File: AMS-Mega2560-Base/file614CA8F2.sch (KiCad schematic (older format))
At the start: 18 parts, among them IC10 LM2917N-8_NOPB, IC9 MAX764CPA+, J20 Conn_01x02, J21 Conn_01x02

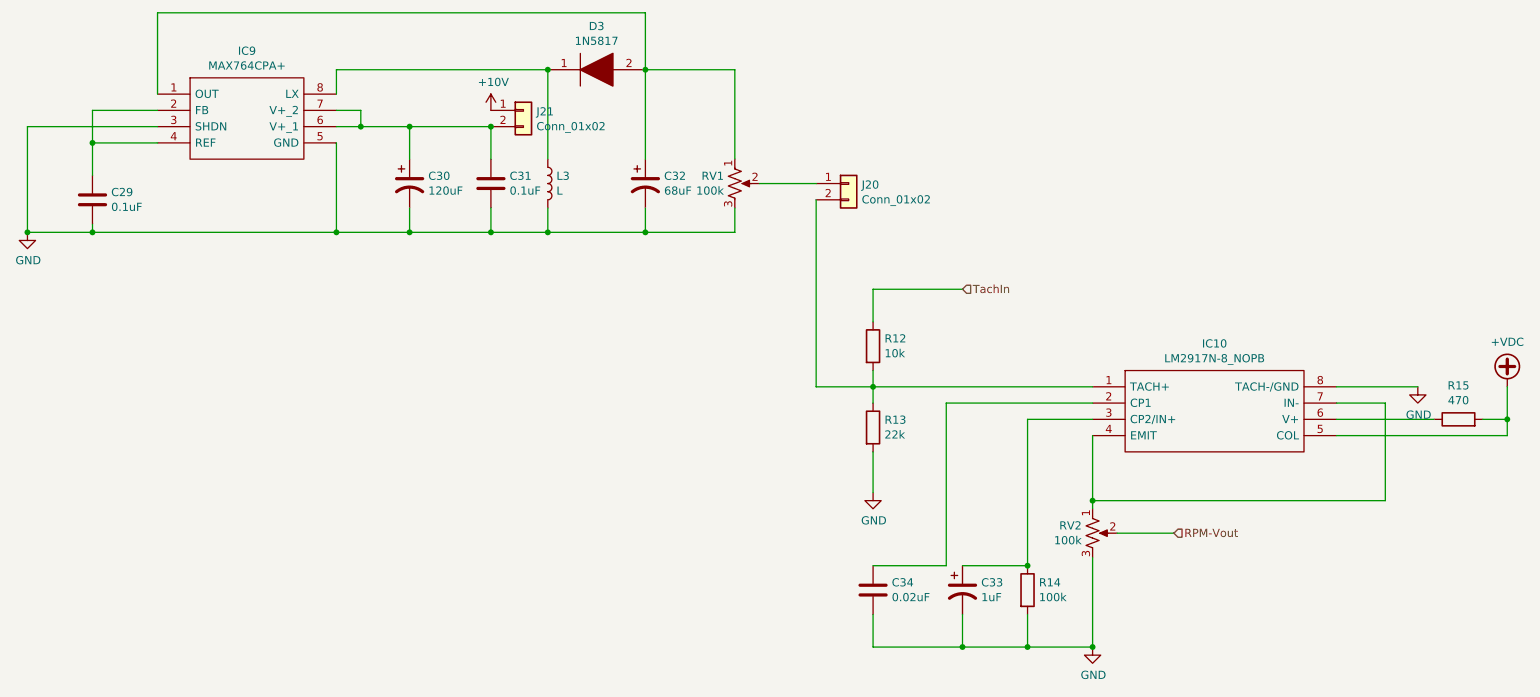
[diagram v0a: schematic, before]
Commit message: rearranging some of the hw design before i rename the repo.
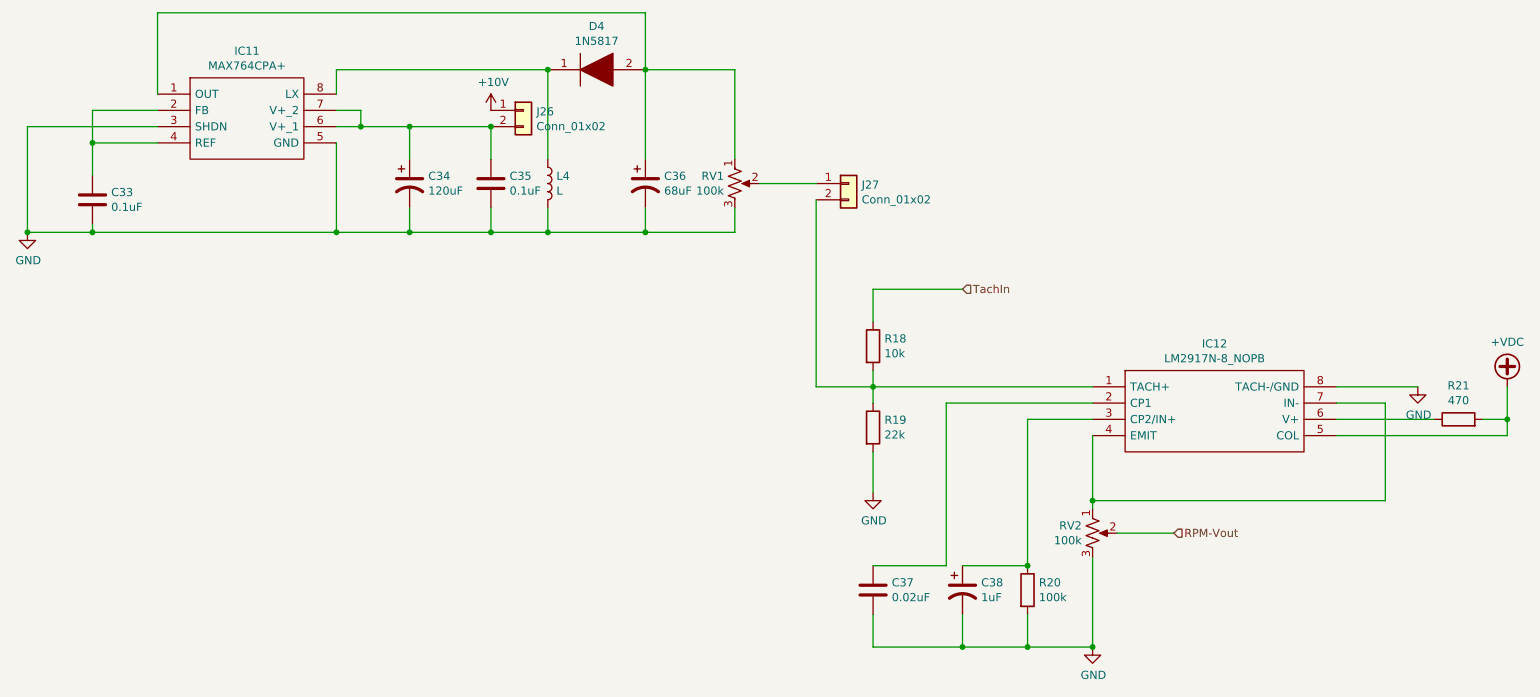
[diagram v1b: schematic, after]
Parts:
- RV1, RV2: footprint Resistor_THT:R_Axial_DIN0207_L6.3mm_D2.5mm_P5.08mm_Vertical -> Potentiometer_THT:Potentiometer_Bourns_3296W_Vertical
- renumbered C29 to C33, C30 to C34, C31 to C35, C32 to C36, C34 to C37, C33 to C38, D3 to D4, IC9 to IC11, IC10 to IC12, J21 to J26, J20 to J27, L3 to L4, R12 to R18, R13 to R19, R14 to R20, R15 to R21
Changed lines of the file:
@@
 $Descr A4 11693 8268
 encoding utf-8
-Sheet 9 13
+Sheet 9 14
 Title ""
 Date ""
@@
 $EndDescr
 $Comp
-L SamacSys_Parts:MAX764CPA+ IC9
+L SamacSys_Parts:MAX764CPA+ IC11
 U 1 1 614CAD3F
 P 1600 1900
-F 0 "IC9" H 2150 2165 50  0000 C CNN
+F 0 "IC11" H 2150 2165 50  0000 C CNN
 F 1 "MAX764CPA+" H 2150 2074 50  0000 C CNN
 F 2 "SamacSys_Parts:DIP762W56P254L938H457Q8N" H 2550 2000 50  0001 L CNN
@@
 $EndComp
 $Comp
-L power:GND #PWR052
+L power:GND #PWR075
 U 1 1 614CDD35
 P 800 2750
-F 0 "#PWR052" H 800 2500 50  0001 C CNN
+F 0 "#PWR075" H 800 2500 50  0001 C CNN
 F 1 "GND" H 805 2577 50  0000 C CNN
 F 2 "" H 800 2750 50  0001 C CNN
@@
 $EndComp
 $Comp
-L power:+10V #PWR053
+L power:+10V #PWR076
 U 1 1 614CE2E3
 P 3650 2000
-F 0 "#PWR053" H 3650 1850 50  0001 C CNN
+F 0 "#PWR076" H 3650 1850 50  0001 C CNN
 F 1 "+10V" H 3665 2173 50  0000 C CNN
 F 2 "" H 3650 2000 50  0001 C CNN
@@
 $EndComp
 $Comp
-L power:+VDC #PWR057
+L power:+VDC #PWR080
 U 1 1 614CE8BE
 P 9900 3700
-F 0 "#PWR057" H 9900 3600 50  0001 C CNN
+F 0 "#PWR080" H 9900 3600 50  0001 C CNN
 F 1 "+VDC" H 9900 3975 50  0000 C CNN
 F 2 "" H 9900 3700 50  0001 C CNN
@@
 $EndComp
 $Comp
-L Device:C C29
+L Device:C C33
 U 1 1 614CFBFE
 P 1200 2550
-F 0 "C29" H 1315 2596 50  0000 L CNN
+F 0 "C33" H 1315 2596 50  0000 L CNN
 F 1 "0.1uF" H 1315 2505 50  0000 L CNN
 F 2 "Capacitor_THT:C_Disc_D7.5mm_W5.0mm_P10.00mm" H 1238 2400 50  0001 C CNN
@@
 Connection ~ 1200 2750
 $Comp
-L Device:CP1 C30
+L Device:CP1 C34
 U 1 1 614D3042
 P 3150 2450
-F 0 "C30" H 3265 2496 50  0000 L CNN
+F 0 "C34" H 3265 2496 50  0000 L CNN
 F 1 "120uF" H 3265 2405 50  0000 L CNN
 F 2 "Capacitor_THT:CP_Radial_D10.0mm_P2.50mm_P5.00mm" H 3150 2450 50  0001 C CNN
@@
 $EndComp
 $Comp
-L Device:C C31
+L Device:C C35
 U 1 1 614D3FE4
 P 3650 2450
-F 0 "C31" H 3765 2496 50  0000 L CNN
+F 0 "C35" H 3765 2496 50  0000 L CNN
 F 1 "0.1uF" H 3765 2405 50  0000 L CNN
 F 2 "Capacitor_THT:C_Disc_D7.5mm_W5.0mm_P10.00mm" H 3688 2300 50  0001 C CNN
@@
 Connection ~ 3650 2750
 $Comp
-L SamacSys_Parts:1N5817 D3
+L SamacSys_Parts:1N5817 D4
 U 1 1 614D9CC2
 P 4000 1750
-F 0 "D3" H 4300 2017 50  0000 C CNN
+F 0 "D4" H 4300 2017 50  0000 C CNN
 F 1 "1N5817" H 4300 1926 50  0000 C CNN
 F 2 "SamacSys_Parts:DIOAD1414W86L464D238" H 4450 1750 50  0001 L CNN
@@
 	4000 2750 4000 2600
 $Comp
-L Device:L L3
+L Device:L L4
 U 1 1 614D76E2
 P 4000 2450
-F 0 "L3" H 4053 2496 50  0000 L CNN
+F 0 "L4" H 4053 2496 50  0000 L CNN
 F 1 "L" H 4053 2405 50  0000 L CNN
 F 2 "Inductor_THT:L_Axial_L7.0mm_D3.3mm_P10.16mm_Horizontal_Fastron_MICC" H 4000 2450 50  0001 C CNN
@@
 	4600 2750 4600 2600
 $Comp
-L Device:CP1 C32
+L Device:CP1 C36
 U 1 1 614D07C1
 P 4600 2450
-F 0 "C32" H 4715 2496 50  0000 L CNN
+F 0 "C36" H 4715 2496 50  0000 L CNN
 F 1 "68uF" H 4715 2405 50  0000 L CNN
 F 2 "Capacitor_THT:CP_Radial_D10.0mm_P2.50mm_P5.00mm" H 4600 2450 50  0001 C CNN
@@
 F 0 "RV1" H 5083 2496 50  0000 R CNN
 F 1 "100k" H 5083 2405 50  0000 R CNN
-F 2 "Resistor_THT:R_Axial_DIN0207_L6.3mm_D2.5mm_P5.08mm_Vertical" H 5150 2450 50  0001 C CNN
+F 2 "Potentiometer_THT:Potentiometer_Bourns_3296W_Vertical" H 5150 2450 50  0001 C CNN
 F 3 "~" H 5150 2450 50  0001 C CNN
 	1    5150 2450
@@
 $EndComp
 $Comp
-L Device:R R12
+L Device:R R18
 U 1 1 614F05B1
 P 6000 3450
-F 0 "R12" H 6070 3496 50  0000 L CNN
+F 0 "R18" H 6070 3496 50  0000 L CNN
 F 1 "10k" H 6070 3405 50  0000 L CNN
 F 2 "Resistor_THT:R_Axial_DIN0207_L6.3mm_D2.5mm_P5.08mm_Vertical" V 5930 3450 50  0001 C CNN
@@
 $EndComp
 $Comp
-L Device:R R13
+L Device:R R19
 U 1 1 614F27D1
 P 6000 3950
-F 0 "R13" H 6070 3996 50  0000 L CNN
+F 0 "R19" H 6070 3996 50  0000 L CNN
 F 1 "22k" H 6070 3905 50  0000 L CNN
 F 2 "Resistor_THT:R_Axial_DIN0207_L6.3mm_D2.5mm_P5.08mm_Vertical" V 5930 3950 50  0001 C CNN
@@
 	6000 3700 6000 3800
 $Comp
-L power:GND #PWR054
+L power:GND #PWR077
 U 1 1 614F5FB8
 P 6000 4350
-F 0 "#PWR054" H 6000 4100 50  0001 C CNN
+F 0 "#PWR077" H 6000 4100 50  0001 C CNN
 F 1 "GND" H 6005 4177 50  0000 C CNN
 F 2 "" H 6000 4350 50  0001 C CNN
@@
 	6000 4350 6000 4100
 $Comp
-L power:GND #PWR056
+L power:GND #PWR079
 U 1 1 614F72BA
 P 9350 3700
-F 0 "#PWR056" H 9350 3450 50  0001 C CNN
+F 0 "#PWR079" H 9350 3450 50  0001 C CNN
 F 1 "GND" H 9355 3527 50  0000 C CNN
 F 2 "" H 9350 3700 50  0001 C CNN
@@
 F 0 "RV2" H 7283 4646 50  0000 R CNN
 F 1 "100k" H 7283 4555 50  0000 R CNN
-F 2 "Resistor_THT:R_Axial_DIN0207_L6.3mm_D2.5mm_P5.08mm_Vertical" H 7350 4600 50  0001 C CNN
+F 2 "Potentiometer_THT:Potentiometer_Bourns_3296W_Vertical" H 7350 4600 50  0001 C CNN
 F 3 "~" H 7350 4600 50  0001 C CNN
 	1    7350 4600
@@
 Connection ~ 7350 4400
 $Comp
-L power:GND #PWR055
+L power:GND #PWR078
 U 1 1 614FC22F
 P 7350 5300
-F 0 "#PWR055" H 7350 5050 50  0001 C CNN
+F 0 "#PWR078" H 7350 5050 50  0001 C CNN
 F 1 "GND" H 7355 5127 50  0000 C CNN
 F 2 "" H 7350 5300 50  0001 C CNN
@@
 $EndComp
 $Comp
-L Device:R R15
+L Device:R R21
 U 1 1 614FDAD7
 P 9600 3900
-F 0 "R15" V 9807 3900 50  0000 C CNN
+F 0 "R21" V 9807 3900 50  0000 C CNN
 F 1 "470" V 9716 3900 50  0000 C CNN
 F 2 "Resistor_THT:R_Axial_DIN0207_L6.3mm_D2.5mm_P5.08mm_Vertical" V 9530 3900 50  0001 C CNN
@@
 	8850 3900 9450 3900
 $Comp
-L SamacSys_Parts:LM2917N-8_NOPB IC10
+L SamacSys_Parts:LM2917N-8_NOPB IC12
 U 1 1 614CC3DD
 P 7350 3700
-F 0 "IC10" H 8100 3965 50  0000 C CNN
+F 0 "IC12" H 8100 3965 50  0000 C CNN
 F 1 "LM2917N-8_NOPB" H 8100 3874 50  0000 C CNN
 F 2 "SamacSys_Parts:DIP794W53P254L959H508Q8N" H 8700 3800 50  0001 L CNN
@@
 	9900 3900 9900 3700
 $Comp
-L Device:R R14
+L Device:R R20
 U 1 1 61508C88
 P 6950 4950
-F 0 "R14" H 7020 4996 50  0000 L CNN
+F 0 "R20" H 7020 4996 50  0000 L CNN
 F 1 "100k" H 7020 4905 50  0000 L CNN
 F 2 "Resistor_THT:R_Axial_DIN0207_L6.3mm_D2.5mm_P5.08mm_Vertical" V 6880 4950 50  0001 C CNN
@@
 $EndComp
 $Comp
-L Device:CP1 C33
+L Device:CP1 C38
 U 1 1 61509D30
 P 6550 4950
-F 0 "C33" H 6665 4996 50  0000 L CNN
+F 0 "C38" H 6665 4996 50  0000 L CNN
 F 1 "1uF" H 6665 4905 50  0000 L CNN
 F 2 "Capacitor_THT:CP_Radial_D7.5mm_P2.50mm" H 6550 4950 50  0001 C CNN
@@
 	6000 3100 6000 3300
 $Comp
-L Connector_Generic:Conn_01x02 J20
+L Connector_Generic:Conn_01x02 J27
 U 1 1 614E1CA5
 P 5850 2450
-F 0 "J20" H 5930 2442 50  0000 L CNN
+F 0 "J27" H 5930 2442 50  0000 L CNN
 F 1 "Conn_01x02" H 5930 2351 50  0000 L CNN
 F 2 "Connector_PinHeader_2.54mm:PinHeader_1x02_P2.54mm_Vertical" H 5850 2450 50  0001 C CNN
@@
 $EndComp
 $Comp
-L Connector_Generic:Conn_01x02 J21
+L Connector_Generic:Conn_01x02 J26
 U 1 1 6151AC67
 P 3850 2000
-F 0 "J21" H 3930 1992 50  0000 L CNN
+F 0 "J26" H 3930 1992 50  0000 L CNN
 F 1 "Conn_01x02" H 3930 1901 50  0000 L CNN
 F 2 "Connector_PinHeader_2.54mm:PinHeader_1x02_P2.54mm_Vertical" H 3850 2000 50  0001 C CNN
@@
 Connection ~ 3650 2100
 $Comp
-L Device:C C34
+L Device:C C37
 U 1 1 615205F8
 P 6000 4950
-F 0 "C34" H 6115 4996 50  0000 L CNN
+F 0 "C37" H 6115 4996 50  0000 L CNN
 F 1 "0.02uF" H 6115 4905 50  0000 L CNN
 F 2 "Capacitor_Tantalum_SMD:CP_EIA-3528-15_AVX-H_Pad1.50x2.35mm_HandSolder" H 6038 4800 50  0001 C CNN
